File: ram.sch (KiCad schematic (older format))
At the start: 4 parts, among them U4 XX4256, U5 XX4256

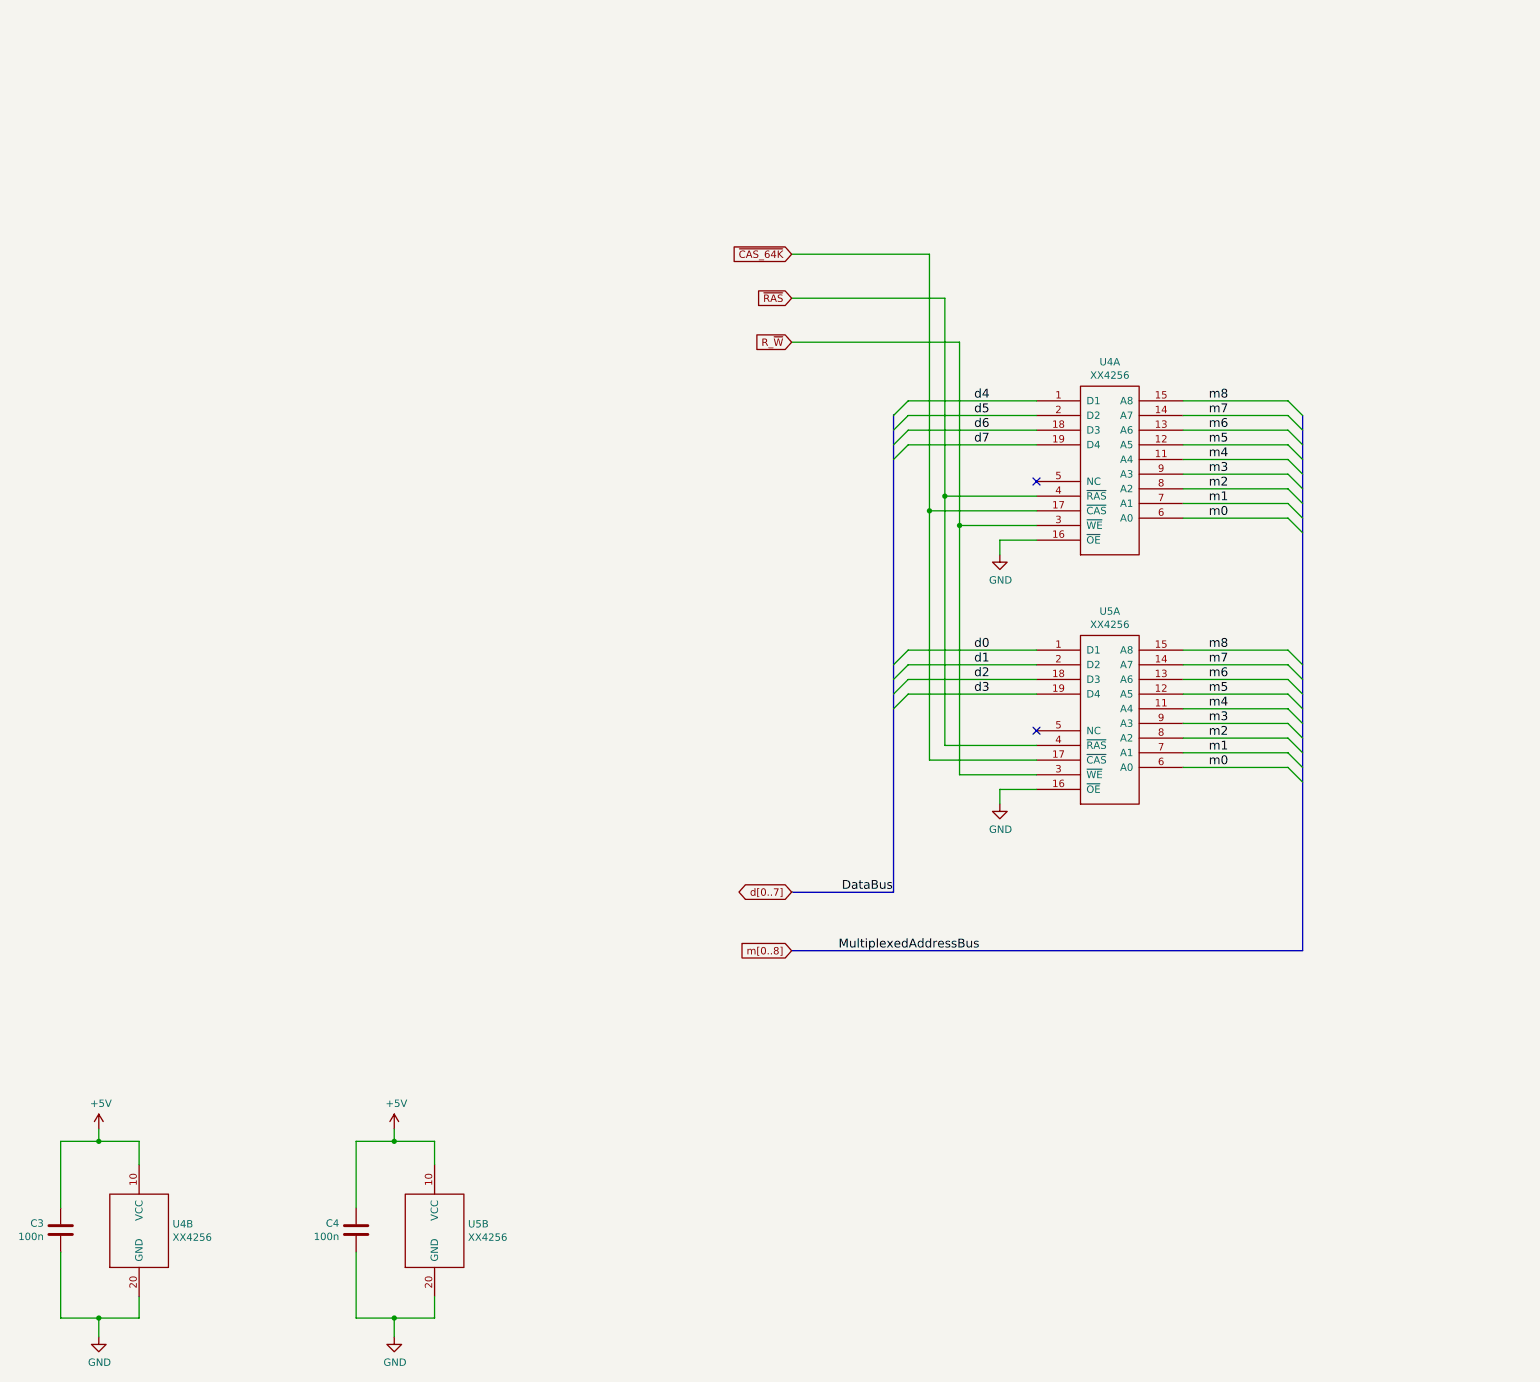
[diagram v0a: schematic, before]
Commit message: Switch to 41256 RAM This will handle the refresh properly despite needing 8 chips instead of 2, sigh...
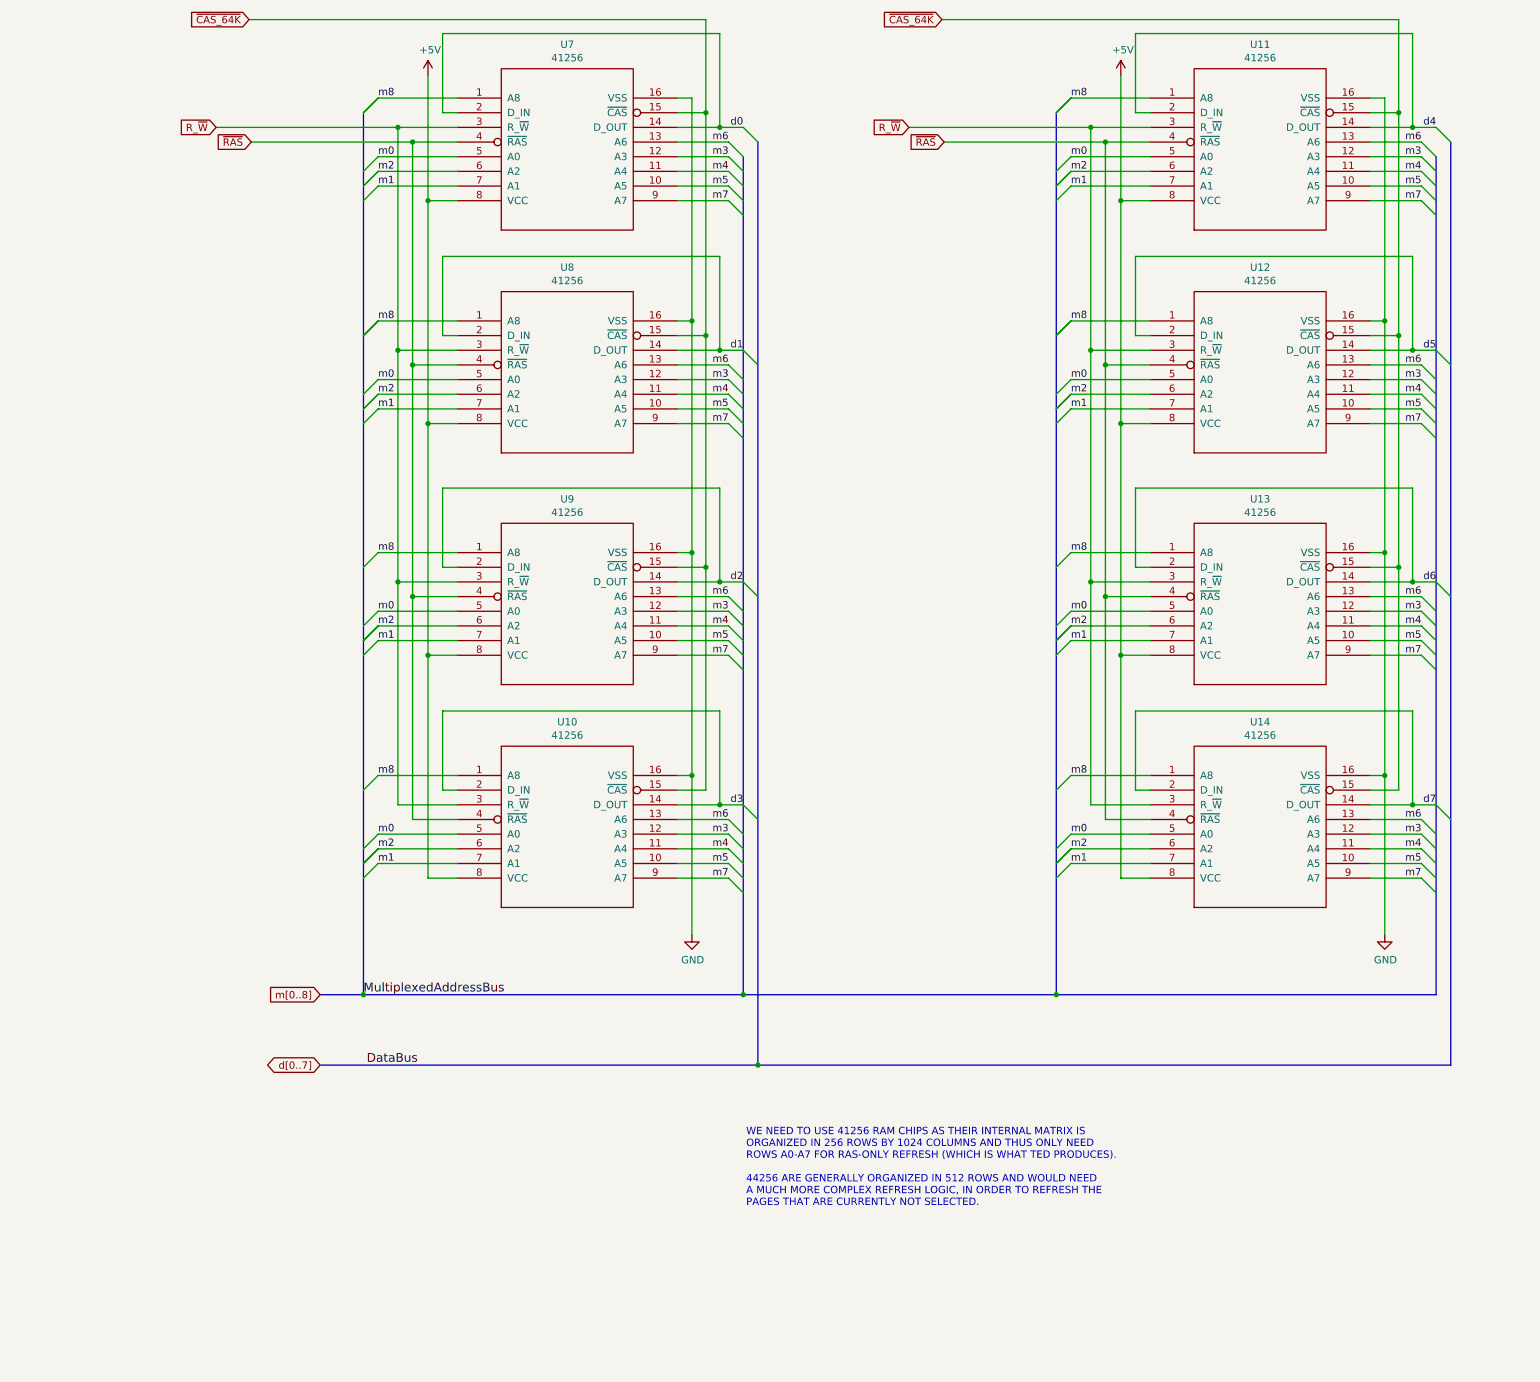
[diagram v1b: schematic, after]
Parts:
- removed C3, C4: 100n, Capacitor_SMD:C_0805_2012Metric_Pad1.18x1.45mm_HandSolder, symbol Device:C
- removed U4, U5: XX4256, Package_DIP:DIP-20_W7.62mm_Socket, symbol XX4256:XX4256
- added U10, U11, U12, U13, U14, U7, U8, U9: 41256, Package_DIP:DIP-16_W7.62mm_Socket, symbol 41256:41256
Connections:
- net +5V: now also U10.8 (VCC), U11.8 (VCC), U12.8 (VCC), U13.8 (VCC), U14.8 (VCC), U7.8 (VCC), U8.8 (VCC), U9.8 (VCC)
- net GND: now also U10.16 (VSS), U11.16 (VSS), U12.16 (VSS), U13.16 (VSS), U14.16 (VSS), U7.16 (VSS), U8.16 (VSS), U9.16 (VSS)
- net R_~W: now also U10.3 (R_~W), U11.3 (R_~W), U12.3 (R_~W), U13.3 (R_~W), U14.3 (R_~W), U7.3 (R_~W), U8.3 (R_~W), U9.3 (R_~W)
- net d0: now also U7.14 (D_OUT), U7.2 (D_IN)
- net d1: now also U8.14 (D_OUT), U8.2 (D_IN)
- net d2: now also U9.14 (D_OUT), U9.2 (D_IN)
- net d3: now also U10.14 (D_OUT), U10.2 (D_IN)
- net d4: now also U11.14 (D_OUT), U11.2 (D_IN)
- net d5: now also U12.14 (D_OUT), U12.2 (D_IN)
- net d6: now also U13.14 (D_OUT), U13.2 (D_IN)
- net d7: now also U14.14 (D_OUT), U14.2 (D_IN)
- net m0: now also U10.5 (A0), U11.5 (A0), U12.5 (A0), U13.5 (A0), U14.5 (A0), U7.5 (A0), U8.5 (A0), U9.5 (A0)
- net m1: now also U10.7 (A1), U11.7 (A1), U12.7 (A1), U13.7 (A1), U14.7 (A1), U7.7 (A1), U8.7 (A1), U9.7 (A1)
- net m2: now also U10.6 (A2), U11.6 (A2), U12.6 (A2), U13.6 (A2), U14.6 (A2), U7.6 (A2), U8.6 (A2), U9.6 (A2)
- net m3: now also U10.12 (A3), U11.12 (A3), U12.12 (A3), U13.12 (A3), U14.12 (A3), U7.12 (A3), U8.12 (A3), U9.12 (A3)
- net m4: now also U10.11 (A4), U11.11 (A4), U12.11 (A4), U13.11 (A4), U14.11 (A4), U7.11 (A4), U8.11 (A4), U9.11 (A4)
- net m5: now also U10.10 (A5), U11.10 (A5), U12.10 (A5), U13.10 (A5), U14.10 (A5), U7.10 (A5), U8.10 (A5), U9.10 (A5)
- net m6: now also U10.13 (A6), U11.13 (A6), U12.13 (A6), U13.13 (A6), U14.13 (A6), U7.13 (A6), U8.13 (A6), U9.13 (A6)
- net m7: now also U10.9 (A7), U11.9 (A7), U12.9 (A7), U13.9 (A7), U14.9 (A7), U7.9 (A7), U8.9 (A7), U9.9 (A7)
- net m8: now also U10.1 (A8), U11.1 (A8), U12.1 (A8), U13.1 (A8), U14.1 (A8), U7.1 (A8), U8.1 (A8), U9.1 (A8)
- net ~CAS_64K: now also U10.15 (~CAS), U11.15 (~CAS), U12.15 (~CAS), U13.15 (~CAS), U14.15 (~CAS), U7.15 (~CAS), U8.15 (~CAS), U9.15 (~CAS)
- net ~RAS: now also U10.4 (~RAS), U11.4 (~RAS), U12.4 (~RAS), U13.4 (~RAS), U14.4 (~RAS), U7.4 (~RAS), U8.4 (~RAS), U9.4 (~RAS)
- no-connect marks 2 -> 0
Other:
- note added: "WE NEED TO USE 41256 RAM CHIPS AS THEIR INTERNAL MATRIX IS\nORGANIZED IN 256 ROWS BY 1024 COLUMNS AND THUS ONLY NEED\nROWS A0-A7 FOR RAS-ONLY REFRESH (WHICH IS WHAT TED PRODUCES).\n\n44256 ARE GENERALLY ORGANIZED IN 512 ROWS AND WOULD NEED\nA MUCH MORE COMPLEX REFRESH LOGIC, IN ORDER TO REFRESH THE\nPAGES THAT ARE CURRENTLY NOT SELECTED."

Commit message: Add credits
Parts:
- added C10, C11, C12, C13, C14, C7, C8, C9: 100n, Capacitor_SMD:C_0805_2012Metric_Pad1.18x1.45mm_HandSolder, symbol Device:C
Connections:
- net +5V: now also C10.1, C11.1, C12.1, C13.1, C14.1, C7.1, C8.1, C9.1
- net GND: now also C10.2, C11.2, C12.2, C13.2, C14.2, C7.2, C8.2, C9.2
